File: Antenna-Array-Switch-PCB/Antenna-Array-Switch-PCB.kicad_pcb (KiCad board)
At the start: 4 copper layers, 98 x 98 mm, 198 parts, among them J1001 Conn_Coaxial, J101 Conn_SMA, J102 Conn_SMA, J103 Conn_SMA, J104 Conn_Coaxial, J201 RFShield_OnePiece, J301 Conn_Coaxial, J401 Conn_Coaxial, J501 Conn_Coaxial, J601 Conn_Coaxial, J701 Conn_Coaxial, J801 Conn_Coaxial, J901 Conn_Coaxial, SW201 TS-1187A-B-A-B, SW202 TS-1187A-B-A-B, U1001 TPS22917DBV, U1002 PGA-103+, U101 LM1117IMP-3.3, U102 SKY13418-485LF, U201 RP2040-Zero, U301 TPS22917DBV, U302 PGA-103+, U401 TPS22917DBV, U402 PGA-103+, U501 TPS22917DBV, U502 PGA-103+, U601 TPS22917DBV, U602 PGA-103+, U701 TPS22917DBV, U702 PGA-103+, U801 TPS22917DBV, U802 PGA-103+, U901 TPS22917DBV, U902 PGA-103+

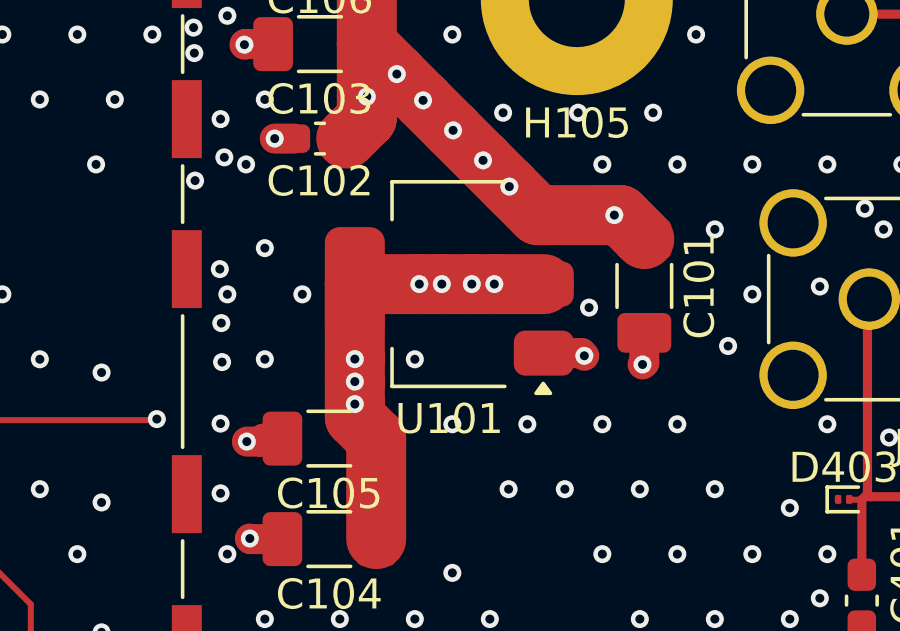
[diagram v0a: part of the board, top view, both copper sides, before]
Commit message: PCB: Update regulator to JLC Basic part
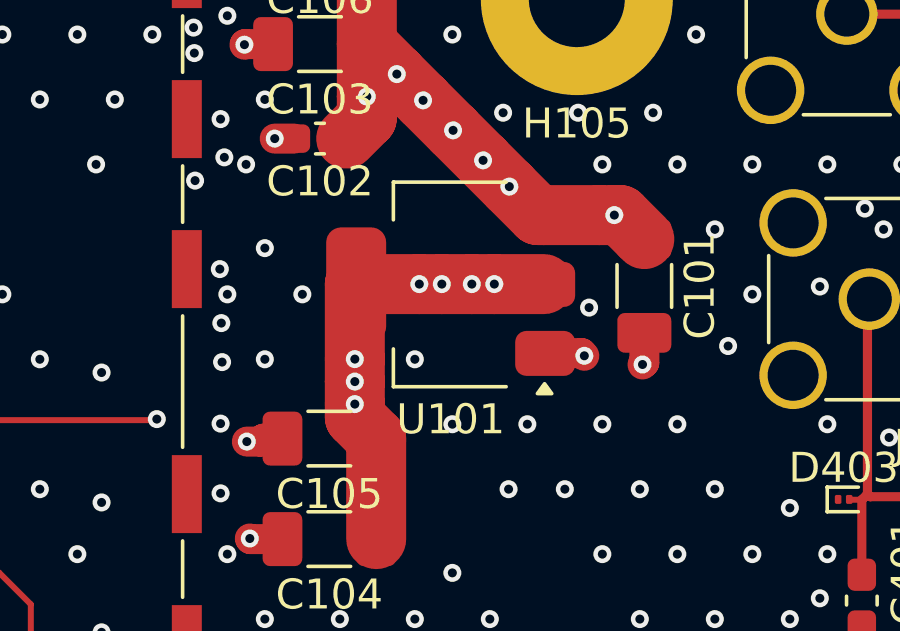
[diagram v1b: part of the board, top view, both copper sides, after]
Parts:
- U101: value LM1117IMP-3.3 -> AMS1117-3.3
